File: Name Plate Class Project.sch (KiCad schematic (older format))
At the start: 0 parts

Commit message: Updates
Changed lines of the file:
@@
 $Descr A4 11693 8268
 encoding utf-8
-Sheet 1 3
+Sheet 1 4
 Title ""
 Date ""
@@
 $EndDescr
 $Sheet
-S 1300 1150 1100 700
+S 1000 1000 1100 700
 U 5EAC05C2
 F0 "Page 1" 50
@@
 $EndSheet
 $Sheet
-S 2750 1150 1100 700
+S 2500 1000 1100 700
 U 5EACA483
 F0 "Page 2" 50
 F1 "Page 2.sch" 50
 $EndSheet
+$Sheet
+S 4000 1000 1100 700
+U 5ECEA271
+F0 "Page 3" 50
+F1 "Page 3.sch" 50
+$EndSheet
 $EndSCHEMATC

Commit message: Updates
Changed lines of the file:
@@
 $Descr A4 11693 8268
 encoding utf-8
-Sheet 1 4
+Sheet 1 10
 Title ""
 Date ""
@@
 F1 "Page 3.sch" 50
 $EndSheet
+$Sheet
+S 5500 1000 1100 700
+U 5ECF2F45
+F0 "Page 4" 50
+F1 "Page 4.sch" 50
+$EndSheet
+$Sheet
+S 7000 1000 1100 700
+U 5ECF2FE7
+F0 "Page 5" 50
+F1 "Page 5.sch" 50
+$EndSheet
+$Sheet
+S 1000 2000 1050 700
+U 5ECF3070
+F0 "Page 6" 50
+F1 "Page 6.sch" 50
+$EndSheet
+$Sheet
+S 2500 2000 1100 700
+U 5ECF3158
+F0 "Page 7" 50
+F1 "Page 7.sch" 50
+$EndSheet
+$Sheet
+S 4000 2000 1100 700
+U 5ECF31FF
+F0 "Page 8" 50
+F1 "Page 8.sch" 50
+$EndSheet
+$Sheet
+S 5500 2000 1100 700
+U 5ECF32A9
+F0 "Page 9" 50
+F1 "Page 9.sch" 50
+$EndSheet
 $EndSCHEMATC

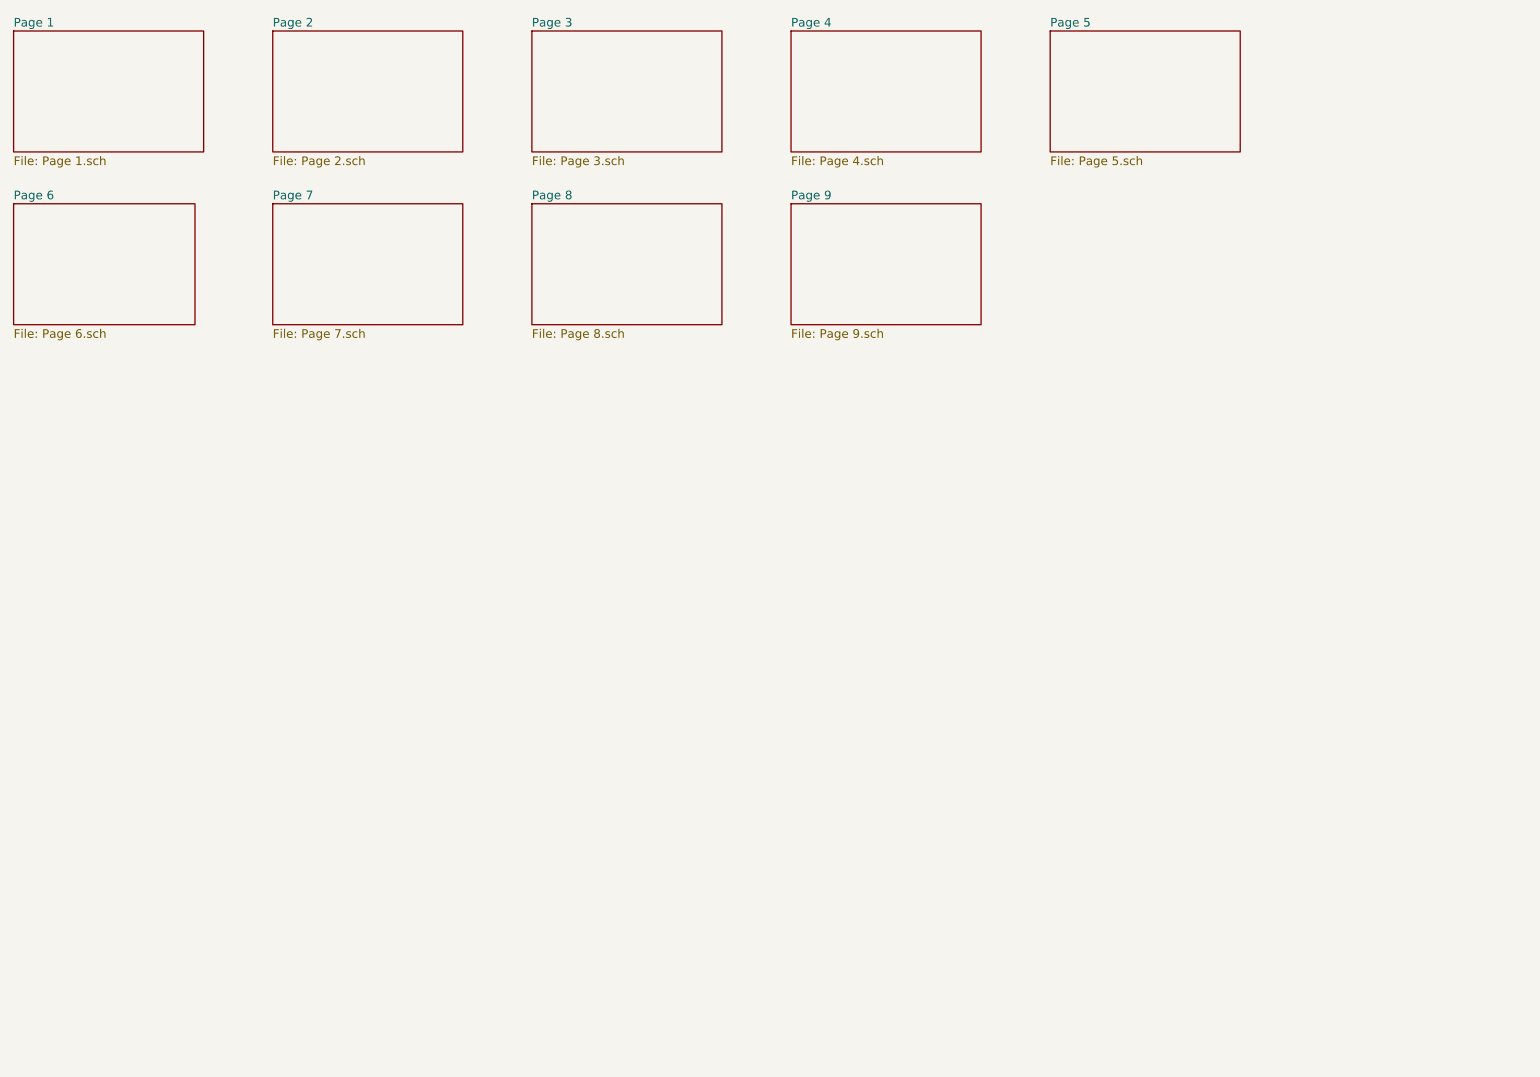
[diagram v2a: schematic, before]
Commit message: Switched to Hierarchical
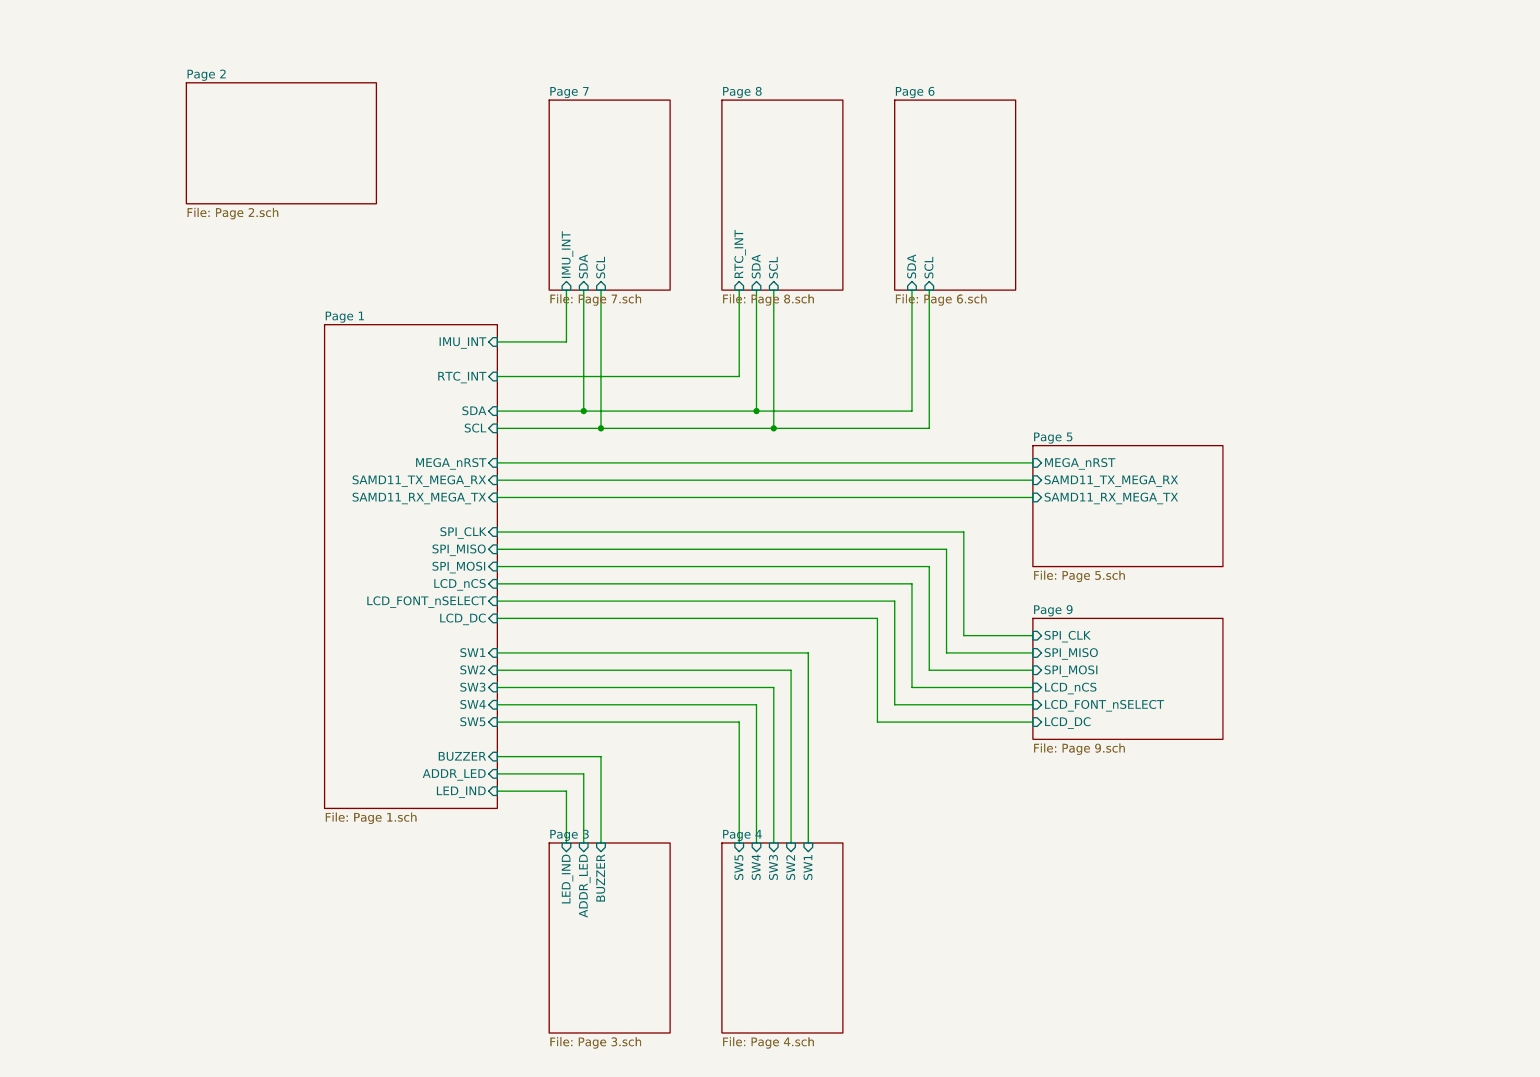
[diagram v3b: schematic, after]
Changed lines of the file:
@@
 $EndDescr
 $Sheet
-S 1000 1000 1100 700
+S 2800 2700 1000 2800
 U 5EAC05C2
 F0 "Page 1" 50
 F1 "Page 1.sch" 50
-$EndSheet
-$Sheet
-S 2500 1000 1100 700
+F2 "IMU_INT" I R 3800 2800 50
+F3 "SDA" I R 3800 3200 50
+F4 "SCL" I R 3800 3300 50
+F5 "SW1" I R 3800 4600 50
+F6 "SW2" I R 3800 4700 50
+F7 "SW3" I R 3800 4800 50
+F8 "SW4" I R 3800 4900 50
+F9 "SW5" I R 3800 5000 50
+F10 "RTC_INT" I R 3800 3000 50
+F11 "MEGA_nRST" I R 3800 3500 50
+F12 "SAMD11_TX_MEGA_RX" I R 3800 3600 50
+F13 "SAMD11_RX_MEGA_TX" I R 3800 3700 50
+F14 "LCD_nCS" I R 3800 4200 50
+F15 "ADDR_LED" I R 3800 5300 50
+F16 "LCD_FONT_nSELECT" I R 3800 4300 50
+F17 "SPI_CLK" I R 3800 3900 50
+F18 "SPI_MISO" I R 3800 4000 50
+F19 "SPI_MOSI" I R 3800 4100 50
+F20 "LCD_DC" I R 3800 4400 50
+F21 "BUZZER" I R 3800 5200 50
+F22 "LED_IND" I R 3800 5400 50
+$EndSheet
+$Sheet
+S 2000 1300 1100 700
 U 5EACA483
 F0 "Page 2" 50
@@
 $EndSheet
 $Sheet
-S 4000 1000 1100 700
+S 4100 5700 700  1100
 U 5ECEA271
 F0 "Page 3" 50
 F1 "Page 3.sch" 50
-$EndSheet
-$Sheet
-S 5500 1000 1100 700
+F2 "BUZZER" I T 4400 5700 50
+F3 "LED_IND" I T 4200 5700 50
+F4 "ADDR_LED" I T 4300 5700 50
+$EndSheet
+$Sheet
+S 5100 5700 700  1100
 U 5ECF2F45
 F0 "Page 4" 50
 F1 "Page 4.sch" 50
-$EndSheet
-$Sheet
-S 7000 1000 1100 700
+F2 "SW1" I T 5600 5700 50
+F3 "SW2" I T 5500 5700 50
+F4 "SW4" I T 5300 5700 50
+F5 "SW5" I T 5200 5700 50
+F6 "SW3" I T 5400 5700 50
+$EndSheet
+$Sheet
+S 6900 3400 1100 700
 U 5ECF2FE7
 F0 "Page 5" 50
 F1 "Page 5.sch" 50
-$EndSheet
-$Sheet
-S 1000 2000 1050 700
+F2 "MEGA_nRST" I L 6900 3500 50
+F3 "SAMD11_TX_MEGA_RX" I L 6900 3600 50
+F4 "SAMD11_RX_MEGA_TX" I L 6900 3700 50
+$EndSheet
+$Sheet
+S 6900 4400 1100 700
+U 5ECF32A9
+F0 "Page 9" 50
+F1 "Page 9.sch" 50
+F2 "SPI_MISO" I L 6900 4600 50
+F3 "LCD_FONT_nSELECT" I L 6900 4900 50
+F4 "SPI_CLK" I L 6900 4500 50
+F5 "SPI_MOSI" I L 6900 4700 50
+F6 "LCD_DC" I L 6900 5000 50
+F7 "LCD_nCS" I L 6900 4800 50
+$EndSheet
+Wire Wire Line
+	4400 3300 5400 3300
+Connection ~ 4400 3300
+Wire Wire Line
+	4400 2500 4400 3300
+Wire Wire Line
+	5400 3300 6300 3300
+Connection ~ 5400 3300
+Wire Wire Line
+	5400 2500 5400 3300
+Wire Wire Line
+	6300 3300 6300 2500
+Wire Wire Line
+	3800 3300 4400 3300
+Wire Wire Line
+	4300 3200 5300 3200
+Connection ~ 4300 3200
+Wire Wire Line
+	3800 3200 4300 3200
+Wire Wire Line
+	4300 2500 4300 3200
+Wire Wire Line
+	5300 3200 6200 3200
+Connection ~ 5300 3200
+Wire Wire Line
+	5300 2500 5300 3200
+Wire Wire Line
+	6200 3200 6200 2500
+Wire Wire Line
+	5200 3000 5200 2500
+Wire Wire Line
+	3800 3000 5200 3000
+Wire Wire Line
+	4200 2500 4200 2800
+$Sheet
+S 5100 1400 700  1100
+U 5ECF31FF
+F0 "Page 8" 50
+F1 "Page 8.sch" 50
+F2 "SCL" I B 5400 2500 50
+F3 "SDA" I B 5300 2500 50
+F4 "RTC_INT" I B 5200 2500 50
+$EndSheet
+Wire Wire Line
+	3800 2800 4200 2800
+$Sheet
+S 4100 1400 700  1100
+U 5ECF3158
+F0 "Page 7" 50
+F1 "Page 7.sch" 50
+F2 "IMU_INT" I B 4200 2500 50
+F3 "SDA" I B 4300 2500 50
+F4 "SCL" I B 4400 2500 50
+$EndSheet
+$Sheet
+S 6100 1400 700  1100
 U 5ECF3070
 F0 "Page 6" 50
 F1 "Page 6.sch" 50
-$EndSheet
-$Sheet
-S 2500 2000 1100 700
-U 5ECF3158
-F0 "Page 7" 50
-F1 "Page 7.sch" 50
-$EndSheet
-$Sheet
-S 4000 2000 1100 700
-U 5ECF31FF
-F0 "Page 8" 50
-F1 "Page 8.sch" 50
-$EndSheet
-$Sheet
-S 5500 2000 1100 700
-U 5ECF32A9
-F0 "Page 9" 50
-F1 "Page 9.sch" 50
-$EndSheet
+F2 "SDA" I B 6200 2500 50
+F3 "SCL" I B 6300 2500 50
+$EndSheet
+Wire Wire Line
+	3800 3500 6900 3500
+Wire Wire Line
+	3800 3600 6900 3600
+Wire Wire Line
+	3800 3700 6900 3700
+Wire Wire Line
+	3800 3900 6500 3900
+Wire Wire Line
+	6500 3900 6500 4500
+Wire Wire Line
+	6500 4500 6900 4500
+Wire Wire Line
+	3800 4000 6400 4000
+Wire Wire Line
+	6400 4000 6400 4600
+Wire Wire Line
+	6400 4600 6900 4600
+Wire Wire Line
+	3800 4100 6300 4100
+Wire Wire Line
+	6300 4100 6300 4700
+Wire Wire Line
+	6300 4700 6900 4700
+Wire Wire Line
+	3800 4200 6200 4200
+Wire Wire Line
+	6200 4200 6200 4800
+Wire Wire Line
+	6200 4800 6900 4800
+Wire Wire Line
+	3800 4300 6100 4300
+Wire Wire Line
+	6100 4300 6100 4900
+Wire Wire Line
+	6100 4900 6900 4900
+Wire Wire Line
+	3800 4400 6000 4400
+Wire Wire Line
+	6000 4400 6000 5000
+Wire Wire Line
+	6000 5000 6900 5000
+Wire Wire Line
+	3800 5400 4200 5400
+Wire Wire Line
+	4200 5400 4200 5700
+Wire Wire Line
+	3800 5300 4300 5300
+Wire Wire Line
+	4300 5300 4300 5700
+Wire Wire Line
+	3800 5200 4400 5200
+Wire Wire Line
+	4400 5200 4400 5700
+Wire Wire Line
+	3800 5000 5200 5000
+Wire Wire Line
+	5200 5000 5200 5700
+Wire Wire Line
+	3800 4900 5300 4900
+Wire Wire Line
+	5300 4900 5300 5700
+Wire Wire Line
+	3800 4800 5400 4800
+Wire Wire Line
+	5400 4800 5400 5700
+Wire Wire Line
+	3800 4700 5500 4700
+Wire Wire Line
+	5500 4700 5500 5700
+Wire Wire Line
+	3800 4600 5600 4600
+Wire Wire Line
+	5600 4600 5600 5700
 $EndSCHEMATC

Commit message: Updating to Final Revision
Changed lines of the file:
@@
 $Descr A4 11693 8268
 encoding utf-8
-Sheet 1 10
+Sheet 1 9
 Title ""
 Date ""
@@
 	4400 2500 4400 3300
 Wire Wire Line
-	5400 3300 6300 3300
-Connection ~ 5400 3300
-Wire Wire Line
 	5400 2500 5400 3300
-Wire Wire Line
-	6300 3300 6300 2500
 Wire Wire Line
 	3800 3300 4400 3300
@@
 	4300 2500 4300 3200
 Wire Wire Line
-	5300 3200 6200 3200
-Connection ~ 5300 3200
-Wire Wire Line
 	5300 2500 5300 3200
-Wire Wire Line
-	6200 3200 6200 2500
 Wire Wire Line
 	5200 3000 5200 2500
@@
 Wire Wire Line
 	3800 2800 4200 2800
+Wire Wire Line
+	3800 3500 6900 3500
+Wire Wire Line
+	3800 3600 6900 3600
+Wire Wire Line
+	3800 3700 6900 3700
+Wire Wire Line
+	3800 3900 6500 3900
+Wire Wire Line
+	6500 3900 6500 4500
+Wire Wire Line
+	6500 4500 6900 4500
+Wire Wire Line
+	3800 4000 6400 4000
+Wire Wire Line
+	6400 4000 6400 4600
+Wire Wire Line
+	6400 4600 6900 4600
+Wire Wire Line
+	3800 4100 6300 4100
+Wire Wire Line
+	6300 4100 6300 4700
+Wire Wire Line
+	6300 4700 6900 4700
+Wire Wire Line
+	3800 4200 6200 4200
+Wire Wire Line
+	6200 4200 6200 4800
+Wire Wire Line
+	6200 4800 6900 4800
+Wire Wire Line
+	3800 4300 6100 4300
+Wire Wire Line
+	6100 4300 6100 4900
+Wire Wire Line
+	6100 4900 6900 4900
+Wire Wire Line
+	3800 4400 6000 4400
+Wire Wire Line
+	6000 4400 6000 5000
+Wire Wire Line
+	6000 5000 6900 5000
+Wire Wire Line
+	3800 5400 4200 5400
+Wire Wire Line
+	4200 5400 4200 5700
+Wire Wire Line
+	3800 5300 4300 5300
+Wire Wire Line
+	4300 5300 4300 5700
+Wire Wire Line
+	3800 5200 4400 5200
+Wire Wire Line
+	4400 5200 4400 5700
+Wire Wire Line
+	3800 5000 5200 5000
+Wire Wire Line
+	5200 5000 5200 5700
+Wire Wire Line
+	3800 4900 5300 4900
+Wire Wire Line
+	5300 4900 5300 5700
+Wire Wire Line
+	3800 4800 5400 4800
+Wire Wire Line
+	5400 4800 5400 5700
+Wire Wire Line
+	3800 4700 5500 4700
+Wire Wire Line
+	5500 4700 5500 5700
+Wire Wire Line
+	3800 4600 5600 4600
+Wire Wire Line
+	5600 4600 5600 5700
 $Sheet
 S 4100 1400 700  1100
-U 5ECF3158
-F0 "Page 7" 50
-F1 "Page 7.sch" 50
-F2 "IMU_INT" I B 4200 2500 50
-F3 "SDA" I B 4300 2500 50
-F4 "SCL" I B 4400 2500 50
-$EndSheet
-$Sheet
-S 6100 1400 700  1100
 U 5ECF3070
 F0 "Page 6" 50
 F1 "Page 6.sch" 50
-F2 "SDA" I B 6200 2500 50
-F3 "SCL" I B 6300 2500 50
-$EndSheet
-Wire Wire Line
-	3800 3500 6900 3500
-Wire Wire Line
-	3800 3600 6900 3600
-Wire Wire Line
-	3800 3700 6900 3700
-Wire Wire Line
-	3800 3900 6500 3900
-Wire Wire Line
-	6500 3900 6500 4500
-Wire Wire Line
-	6500 4500 6900 4500
-Wire Wire Line
-	3800 4000 6400 4000
-Wire Wire Line
-	6400 4000 6400 4600
-Wire Wire Line
-	6400 4600 6900 4600
-Wire Wire Line
-	3800 4100 6300 4100
-Wire Wire Line
-	6300 4100 6300 4700
-Wire Wire Line
-	6300 4700 6900 4700
-Wire Wire Line
-	3800 4200 6200 4200
-Wire Wire Line
-	6200 4200 6200 4800
-Wire Wire Line
-	6200 4800 6900 4800
-Wire Wire Line
-	3800 4300 6100 4300
-Wire Wire Line
-	6100 4300 6100 4900
-Wire Wire Line
-	6100 4900 6900 4900
-Wire Wire Line
-	3800 4400 6000 4400
-Wire Wire Line
-	6000 4400 6000 5000
-Wire Wire Line
-	6000 5000 6900 5000
-Wire Wire Line
-	3800 5400 4200 5400
-Wire Wire Line
-	4200 5400 4200 5700
-Wire Wire Line
-	3800 5300 4300 5300
-Wire Wire Line
-	4300 5300 4300 5700
-Wire Wire Line
-	3800 5200 4400 5200
-Wire Wire Line
-	4400 5200 4400 5700
-Wire Wire Line
-	3800 5000 5200 5000
-Wire Wire Line
-	5200 5000 5200 5700
-Wire Wire Line
-	3800 4900 5300 4900
-Wire Wire Line
-	5300 4900 5300 5700
-Wire Wire Line
-	3800 4800 5400 4800
-Wire Wire Line
-	5400 4800 5400 5700
-Wire Wire Line
-	3800 4700 5500 4700
-Wire Wire Line
-	5500 4700 5500 5700
-Wire Wire Line
-	3800 4600 5600 4600
-Wire Wire Line
-	5600 4600 5600 5700
+F2 "SDA" I B 4300 2500 50
+F3 "SCL" I B 4400 2500 50
+F4 "IMU_INT" I B 4200 2500 50
+$EndSheet
 $EndSCHEMATC

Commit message: Updating Page Numbering
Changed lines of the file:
@@
 F4 "SAMD11_RX_MEGA_TX" I L 6900 3700 50
-$EndSheet
-$Sheet
-S 6900 4400 1100 700
-U 5ECF32A9
-F0 "Page 9" 50
-F1 "Page 9.sch" 50
-F2 "SPI_MISO" I L 6900 4600 50
-F3 "LCD_FONT_nSELECT" I L 6900 4900 50
-F4 "SPI_CLK" I L 6900 4500 50
-F5 "SPI_MOSI" I L 6900 4700 50
-F6 "LCD_DC" I L 6900 5000 50
-F7 "LCD_nCS" I L 6900 4800 50
 $EndSheet
 Wire Wire Line
@@
 Wire Wire Line
 	4200 2500 4200 2800
-$Sheet
-S 5100 1400 700  1100
-U 5ECF31FF
-F0 "Page 8" 50
-F1 "Page 8.sch" 50
-F2 "SCL" I B 5400 2500 50
-F3 "SDA" I B 5300 2500 50
-F4 "RTC_INT" I B 5200 2500 50
-$EndSheet
 Wire Wire Line
 	3800 2800 4200 2800
@@
 F4 "IMU_INT" I B 4200 2500 50
 $EndSheet
+$Sheet
+S 5100 1400 700  1100
+U 5ECF31FF
+F0 "Page 7" 50
+F1 "Page 7.sch" 50
+F2 "SCL" I B 5400 2500 50
+F3 "SDA" I B 5300 2500 50
+F4 "RTC_INT" I B 5200 2500 50
+$EndSheet
+$Sheet
+S 6900 4400 1100 700
+U 5ECF32A9
+F0 "Page 8" 50
+F1 "Page 8.sch" 50
+F2 "SPI_MISO" I L 6900 4600 50
+F3 "LCD_FONT_nSELECT" I L 6900 4900 50
+F4 "SPI_CLK" I L 6900 4500 50
+F5 "SPI_MOSI" I L 6900 4700 50
+F6 "LCD_DC" I L 6900 5000 50
+F7 "LCD_nCS" I L 6900 4800 50
+$EndSheet
 $EndSCHEMATC
